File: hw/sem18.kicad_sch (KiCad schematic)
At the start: 4 parts, among them J3 USB_C_Receptacle_PowerOnly_6P

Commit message: WIP
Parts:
- removed J3: USB_C_Receptacle_PowerOnly_6P, Connector_USB:USB_C_Receptacle_GCT_USB4125-xx-x_6P_TopMnt_Horizontal, symbol Connector:USB_C_Receptacle_PowerOnly_6P
- added J2: USB_C_Receptacle_USB2.0_16P, symbol Connector:USB_C_Receptacle_USB2.0_16P
- added U5: SRV05-4, Package_TO_SOT_SMD:SOT-23-6, symbol Power_Protection:SRV05-4
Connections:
- net GND: now also J2.A1 (GND), J2.A12 (GND), J2.B1 (GND), J2.B12 (GND), J2.S1 (SHIELD), U5.2 (VN)
- net at R9.2: now also J2.A5 (CC1)
- net USB_VBUS: now reaches F1.1
- net USB_VBUS: now also J2.A4 (VBUS), J2.A9 (VBUS), J2.B4 (VBUS), J2.B9 (VBUS), U5.5 (VP)
- net at R8.2: now also J2.B5 (CC2)
- net Power/USBPOWER_IN: now reaches F1.2
- new net MCU/USB_DM: J2.A7 (D-), J2.B7 (D-), U5.1 (IO1), U5.6 (IO4)
- new net MCU/USB_DP: J2.A6 (D+), J2.B6 (D+), U5.3 (IO2), U5.4 (IO3)
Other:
- sheet MCU ports: added USB_DM, USB_DP; removed none
- sheet Power ports: added USBPOWER_IN; removed none
- moved on the sheet: F1, R8, R9

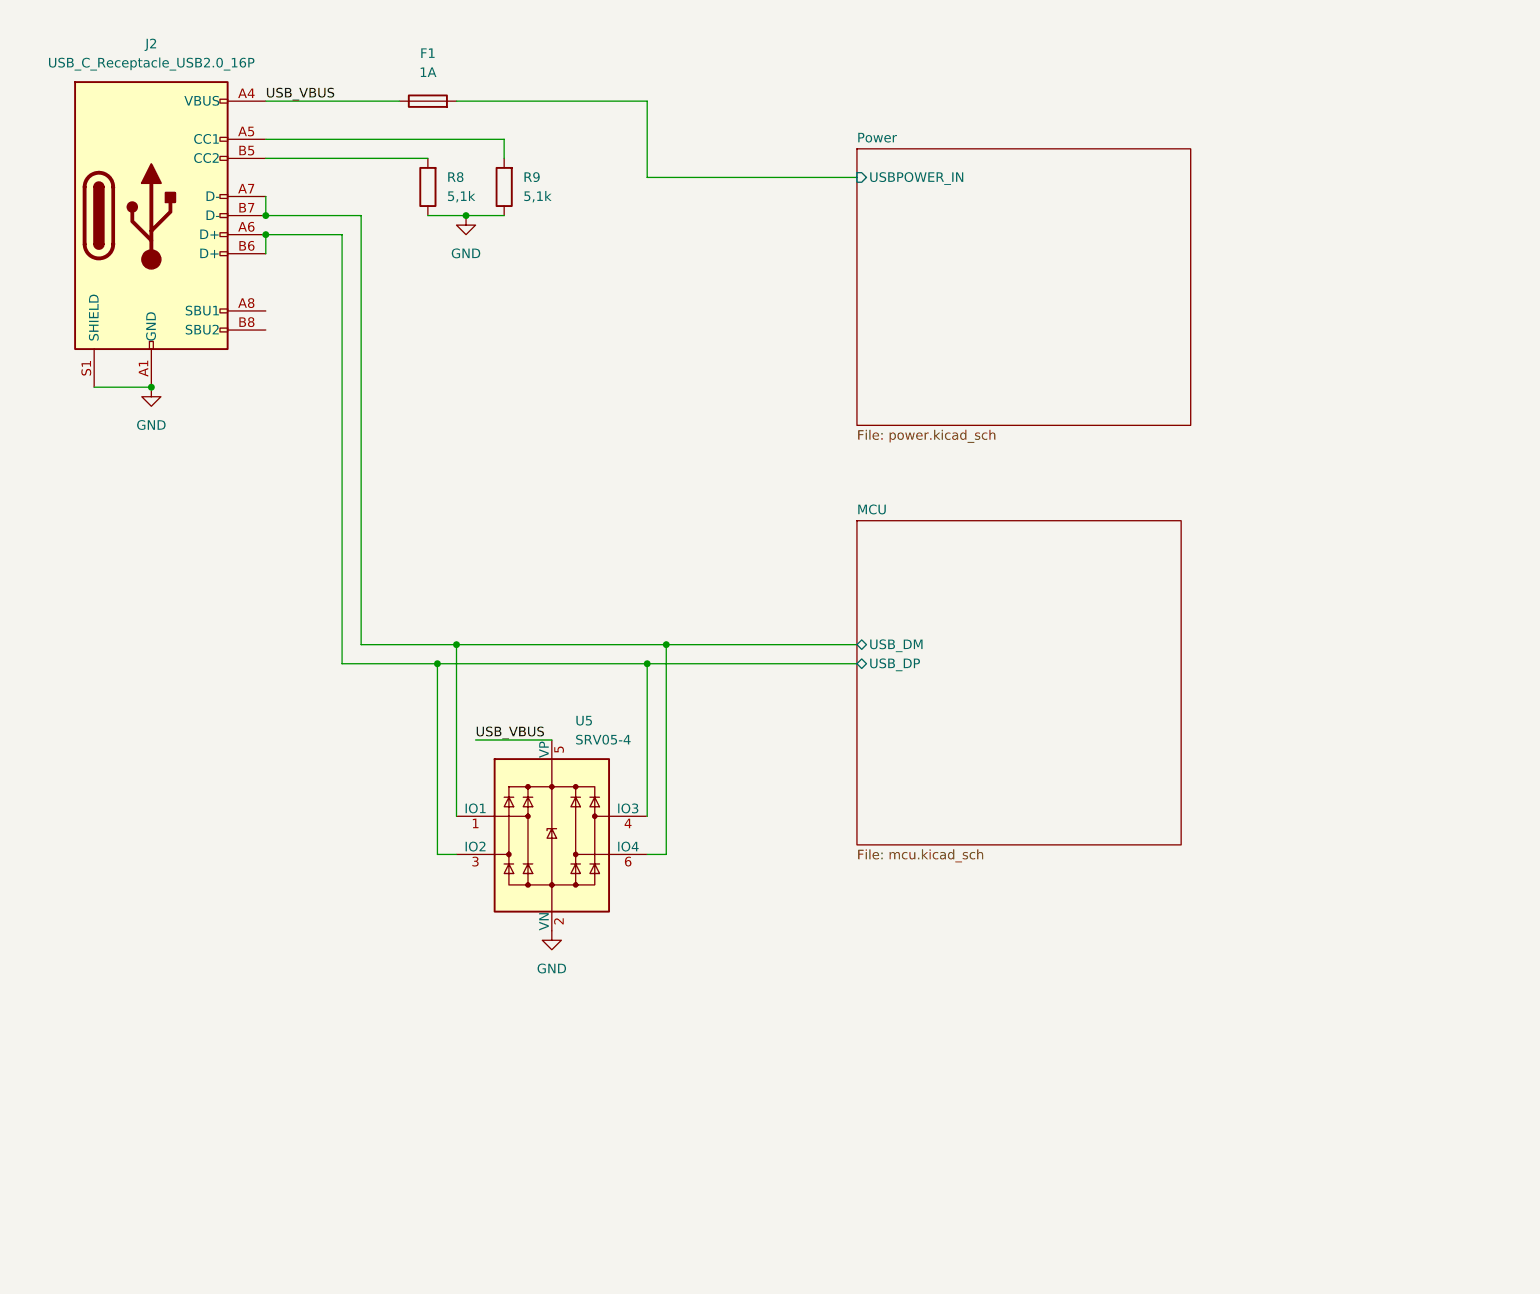
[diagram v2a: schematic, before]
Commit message: Schematic is finished. Needs some touch-ups and component selection (esp. for switches).
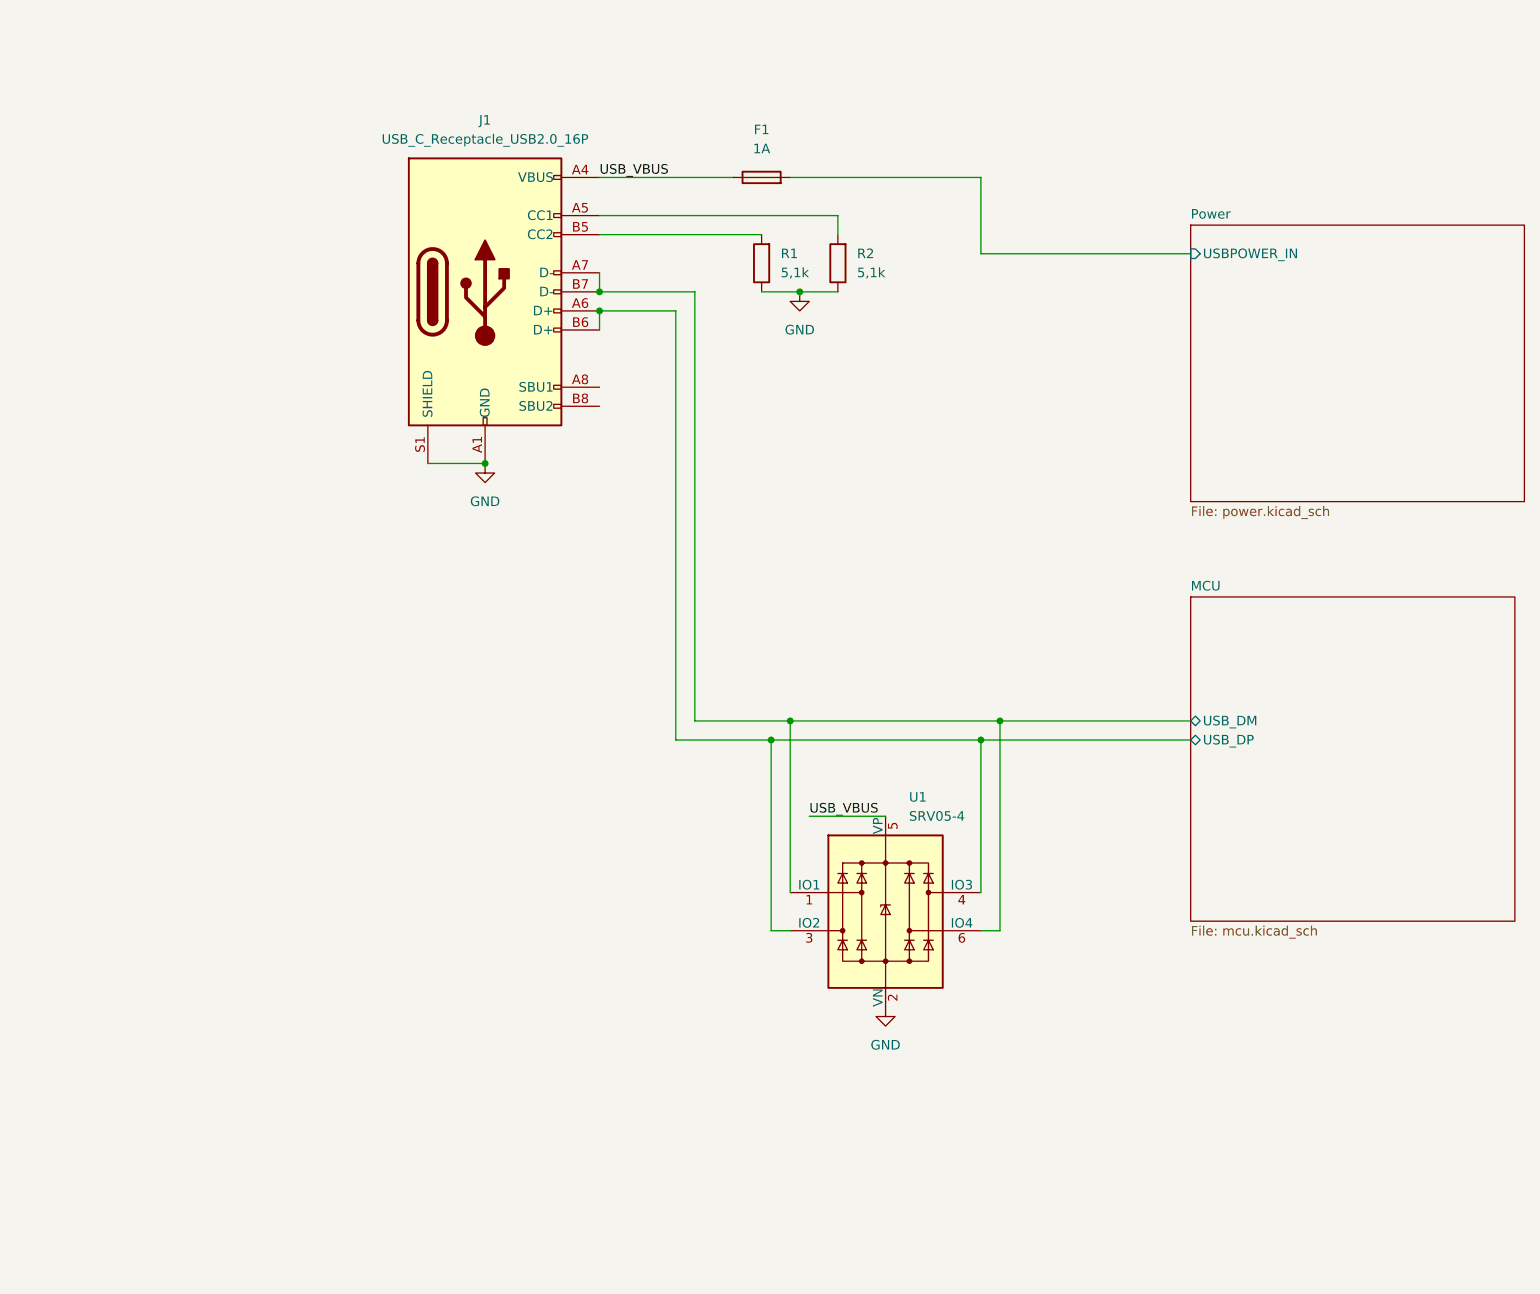
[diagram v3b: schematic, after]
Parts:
- renumbered J2 to J1, R8 to R1, R9 to R2, U5 to U1
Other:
- moved on the sheet: F1, J1, R1, R2, U1

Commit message: WIP
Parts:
- J1: footprint (none) -> Connector_USB:USB_C_Receptacle_G-Switch_GT-USB-7010ASV
- R1, R2: footprint Resistor_SMD:R_0805_2012Metric -> Resistor_SMD:R_0603_1608Metric
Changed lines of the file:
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@@
 			)
 		)
-		(property "Footprint" "Resistor_SMD:R_0805_2012Metric"
+		(property "Footprint" "Resistor_SMD:R_0603_1608Metric"
 			(at 128.778 48.26 90)
 			(effects
@@
 			)
 		)
-		(property "Footprint" ""
+		(property "Footprint" "Connector_USB:USB_C_Receptacle_G-Switch_GT-USB-7010ASV"
 			(at 83.82 52.07 0)
 			(effects
@@
 			)
 		)
-		(property "Footprint" "Resistor_SMD:R_0805_2012Metric"
+		(property "Footprint" "Resistor_SMD:R_0603_1608Metric"
 			(at 118.618 48.26 90)
 			(effects

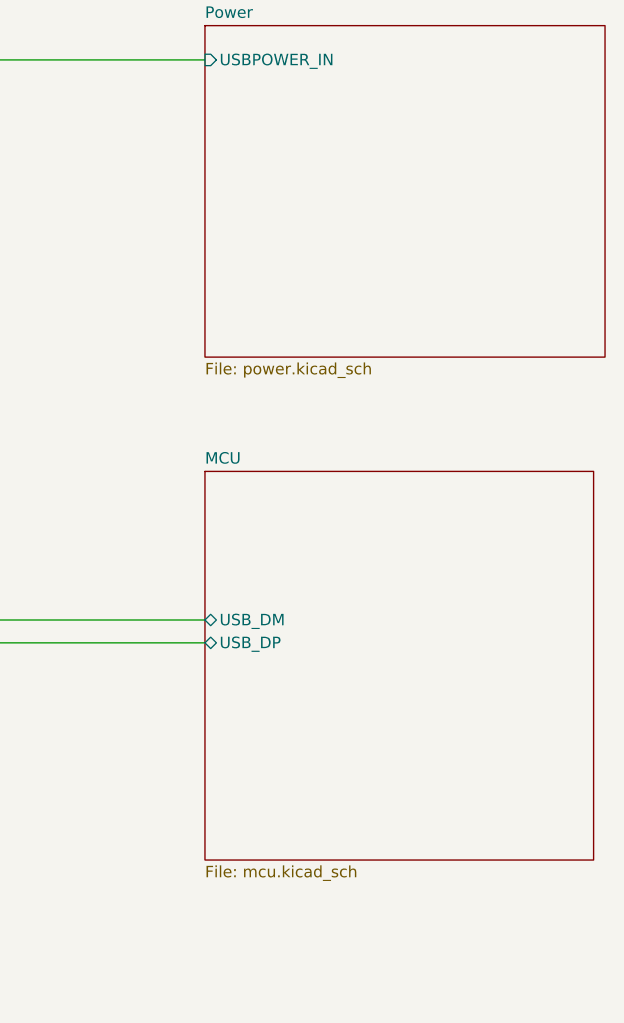
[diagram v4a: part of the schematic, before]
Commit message: Different microcontroller. Placed most of the components too.
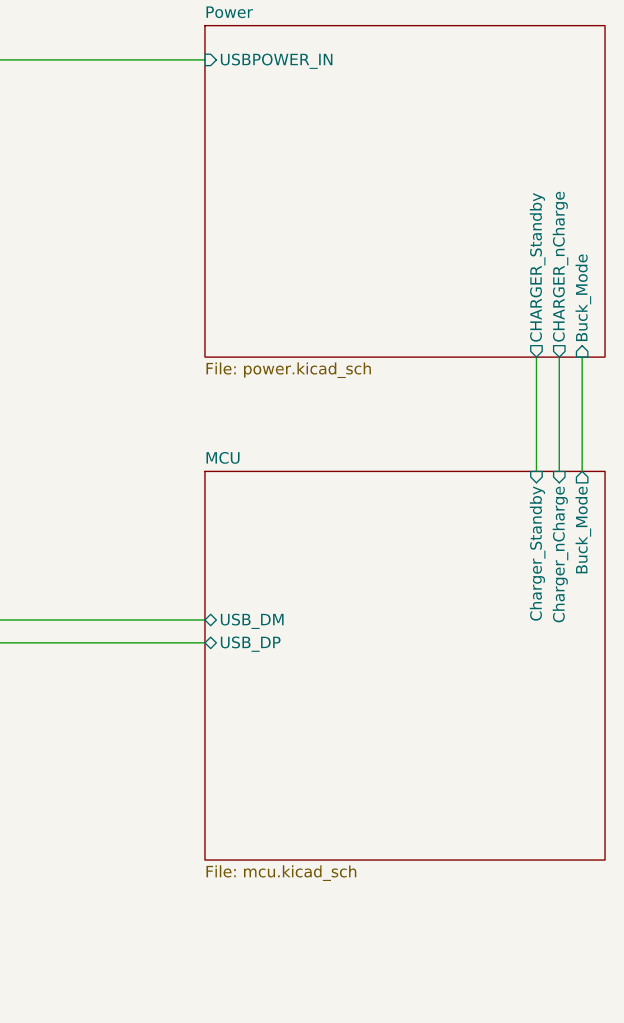
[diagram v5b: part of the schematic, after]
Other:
- sheet MCU ports: added Buck_Mode, Charger_Standby, Charger_nCharge; removed none
- sheet Power ports: added Buck_Mode, CHARGER_Standby, CHARGER_nCharge; removed none
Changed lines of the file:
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@@
+	(wire
+		(pts
+			(xy 213.36 80.01) (xy 213.36 92.71)
+		)
+		(stroke
+			(width 0)
+			(type default)
+		)
+	)
 	(wire
 		(pts
@@
 		(pts
 			(xy 146.05 111.76) (xy 146.05 132.08)
+		)
+		(stroke
+			(width 0)
+			(type default)
+		)
+	)
+	(wire
+		(pts
+			(xy 215.9 80.01) (xy 215.9 92.71)
+		)
+		(stroke
+			(width 0)
+			(type default)
+		)
+	)
+	(wire
+		(pts
+			(xy 210.82 80.01) (xy 210.82 92.71)
 		)
 		(stroke
@@
 			)
 		)
+		(pin "Buck_Mode" input
+			(at 215.9 80.01 270)
+			(effects
+				(font
+					(size 1.27 1.27)
+				)
+				(justify left)
+			)
+		)
+		(pin "CHARGER_nCharge" output
+			(at 213.36 80.01 270)
+			(effects
+				(font
+					(size 1.27 1.27)
+				)
+				(justify left)
+			)
+		)
+		(pin "CHARGER_Standby" output
+			(at 210.82 80.01 270)
+			(effects
+				(font
+					(size 1.27 1.27)
+				)
+				(justify left)
+			)
+		)
 		(instances
 			(project "sem18"
@@
 	(sheet
 		(at 173.99 92.71)
-		(size 43.18 43.18)
+		(size 44.45 43.18)
 		(exclude_from_sim no)
 		(in_bom yes)
@@
 			)
 		)
+		(pin "Buck_Mode" output
+			(at 215.9 92.71 90)
+			(effects
+				(font
+					(size 1.27 1.27)
+				)
+				(justify right)
+			)
+		)
+		(pin "Charger_nCharge" input
+			(at 213.36 92.71 90)
+			(effects
+				(font
+					(size 1.27 1.27)
+				)
+				(justify right)
+			)
+		)
+		(pin "Charger_Standby" input
+			(at 210.82 92.71 90)
+			(effects
+				(font
+					(size 1.27 1.27)
+				)
+				(justify right)
+			)
+		)

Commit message: Sent to fab.
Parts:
- added T1, T2: Tab, PCM_kikit:Tab, symbol PCM_kikit:Tab
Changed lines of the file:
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@@
+	)
+	(symbol
+		(lib_id "PCM_kikit:Tab")
+		(at 40.64 173.99 0)
+		(unit 1)
+		(exclude_from_sim no)
+		(in_bom no)
+		(on_board yes)
+		(dnp no)
+		(fields_autoplaced yes)
+		(property "Reference" "T1"
+			(at 45.72 172.0849 0)
+			(effects
+				(font
+					(size 1.27 1.27)
+				)
+				(justify left)
+			)
+		)
+		(property "Value" "Tab"
+			(at 45.72 174.6249 0)
+			(effects
+				(font
+					(size 1.27 1.27)
+				)
+				(justify left)
+			)
+		)
+		(property "Footprint" "PCM_kikit:Tab"
+			(at 40.64 173.99 0)
+			(effects
+				(font
+					(size 1.27 1.27)
+				)
+				(hide yes)
+			)
+		)
+		(property "Datasheet" ""
+			(at 40.64 173.99 0)
+			(effects
+				(font
+					(size 1.27 1.27)
+				)
+				(hide yes)
+			)
+		)
+		(property "Description" "KiKit tab annotations"
+			(at 40.64 173.99 0)
+			(effects
+				(font
+					(size 1.27 1.27)
+				)
+				(hide yes)
+			)
+		)
+		(instances
+			(project "sem18"
+				(path "/d844aefd-19cf-4889-9465-41f3f1184bf3"
+					(reference "T1")
+					(unit 1)
+				)
+			)
+		)
 	)
 	(symbol
@@
 					(unit 1)
 				)
+			)
+		)
+	)
+	(symbol
+		(lib_id "PCM_kikit:Tab")
+		(at 40.64 181.61 0)
+		(unit 1)
+		(exclude_from_sim no)
+		(in_bom no)
+		(on_board yes)
+		(dnp no)
+		(fields_autoplaced yes)
+		(property "Reference" "T2"
+			(at 45.72 179.7049 0)
+			(effects
+				(font
+					(size 1.27 1.27)
+				)
+				(justify left)
+			)
+		)
+		(property "Value" "Tab"
+			(at 45.72 182.2449 0)
+			(effects
+				(font
+					(size 1.27 1.27)
+				)
+				(justify left)
+			)
+		)
+		(property "Footprint" "PCM_kikit:Tab"
+			(at 40.64 181.61 0)
+			(effects
+				(font
+					(size 1.27 1.27)
+				)
+				(hide yes)
+			)
+		)
+		(property "Datasheet" ""
+			(at 40.64 181.61 0)
+			(effects
+				(font
+					(size 1.27 1.27)
+				)
+				(hide yes)
+			)
+		)
+		(property "Description" "KiKit tab annotations"
+			(at 40.64 181.61 0)
+			(effects
+				(font
+					(size 1.27 1.27)
+				)
+				(hide yes)
+			)
+		)
+		(instances
+			(project "sem18"
+				(path "/d844aefd-19cf-4889-9465-41f3f1184bf3"
+					(reference "T2")
+					(unit 1)
+				)
